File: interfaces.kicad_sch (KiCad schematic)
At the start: 97 parts, among them IC3 TPD8S009DSMR, J5 HDMI-A_685119134923, J6 USB_Micro-B_629105150521, J7 MicroSD_1140084168, Q3 BSS138PW, Q4 BSS138PW, Q5 BSS138PW, Q6 BSS138PW, Q7 BSS138PW, U10 FT4232H_QFN, U34 AT24CS01_SOT23, Y2 Oscillator_SMD_12MHz_KX-7

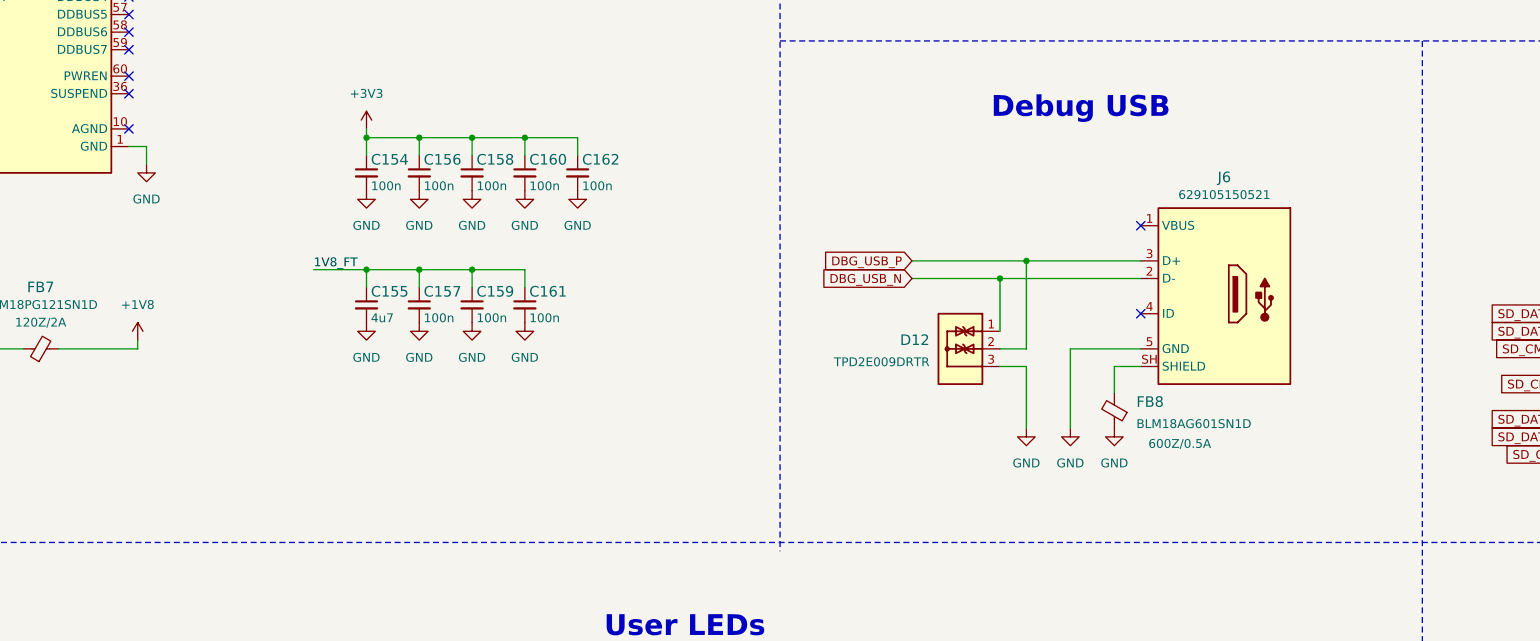
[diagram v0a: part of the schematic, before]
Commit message: [#95002] Change USB to C type
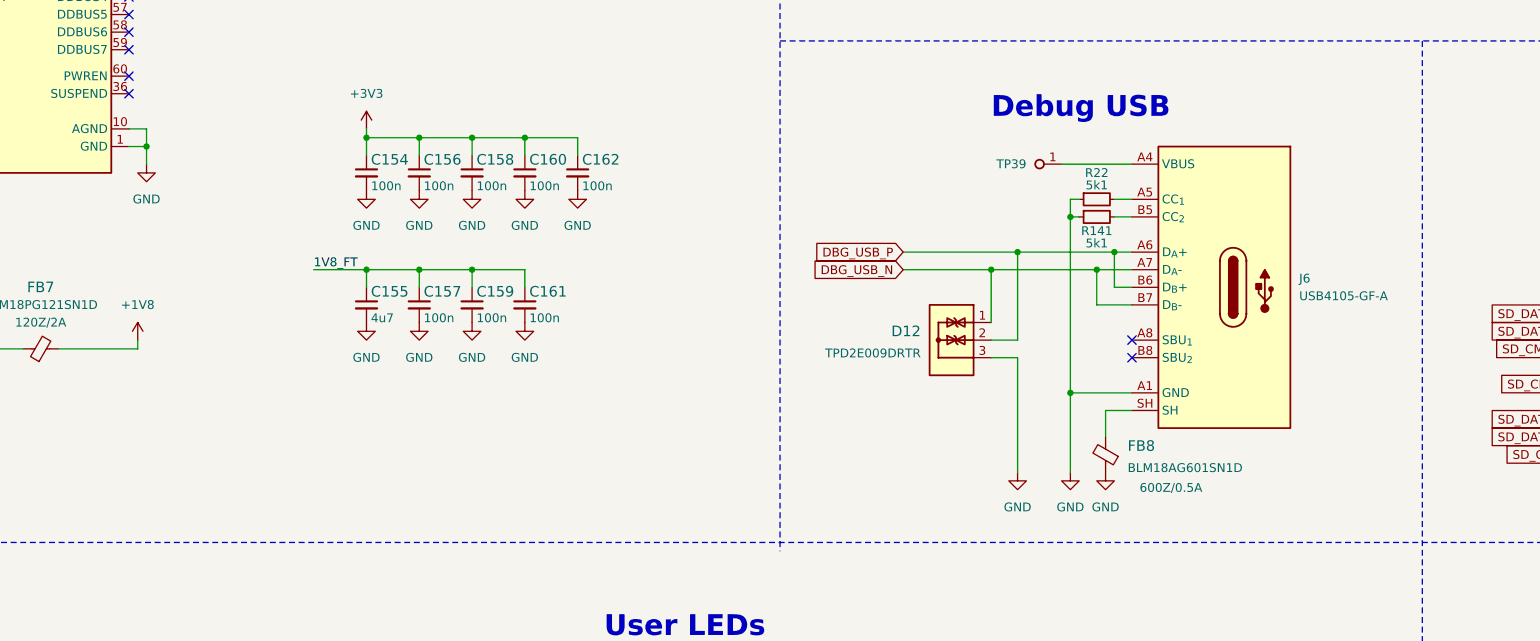
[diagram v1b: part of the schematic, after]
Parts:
- removed J6: USB_Micro-B_629105150521, antmicro-footprints:USB-Micro-B_Receptacle_WE_629105150521, symbol antmicroUSBConnectors:USB-Micro-B_WE_629105150521
- added J6: USB-C_GCT_USB4105-GF-A, antmicro-footprints:USB-C_Receptacle_GCT_USB4105-GF-A, symbol USBConnectors:USB-C_GCT_USB4105-GF-A
- added R141, R22: R_5k1_0402, antmicro-footprints:R_0402_1005Metric, symbol Resistors0402:R_5k1_0402
- added TP39: TP_1mm_SMD, antmicro-footprints:TP_SMD_1mm, symbol antmicroTestPoints:TP_1mm_SMD
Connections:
- net DBG_USB_N: now also J6.A7 (D_{A}-), J6.B7 (D_{B}-)
- net DBG_USB_P: now also J6.A6 (D_{A}+), J6.B6 (D_{B}+)
- net GND: now also U10.10 (AGND), J6.A1 (GND), J6.A12 (GND), J6.B1 (GND), J6.B12 (GND), R141.1, R22.1
- net at FB8.2: now also J6.SH
- new net: J6.A4 (VBUS), J6.A9 (VBUS), J6.B4 (VBUS), J6.B9 (VBUS), TP39.1
- new net: J6.A5 (CC_{1}), R22.2
- new net: J6.B5 (CC_{2}), R141.2
- no-connect marks 27 -> 26
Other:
- moved on the sheet: D12, FB8
